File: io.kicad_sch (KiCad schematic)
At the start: 80 parts, among them IC16 MC1489, IC19 MC1488, IC23 MC1489, IC24 82C711, X7 24MHz

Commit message: prepare for fabrication
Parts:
- C108, C111, C112, C113, C114, C115, C122, C123, C125, C126, C132, C134, C136, C153, C154, C155, C156: LCSC (none) -> C1790; LCSC Part (none) -> C1790
- C127, C133, C135, C141, C142, C143, C144, C145: LCSC (none) -> C46653; LCSC Part (none) -> C46653
- C128, C129: LCSC (none) -> C1804; LCSC Part (none) -> C1804
- C137, C146: LCSC (none) -> C344201; LCSC Part (none) -> C344201
- C147, C158: LCSC (none) -> C49678; LCSC Part (none) -> C49678
- C149: LCSC (none) -> C2987938; LCSC Part (none) -> C2987938
- IC16, IC23: LCSC (none) -> C3199481; LCSC Part (none) -> C3199481
- IC19: LCSC (none) -> C3213152; LCSC Part (none) -> C3213152
- R116, R117, R118, R121, R122, R123, R126, R131, R138, R140, R141: LCSC (none) -> C2907326; LCSC Part (none) -> C2907326
- R119: LCSC (none) -> C2907219; LCSC Part (none) -> C2907219
- R120: LCSC (none) -> C17634; LCSC Part (none) -> C17634
- R127: LCSC (none) -> C5713328; LCSC Part (none) -> C5713328
- R128: LCSC (none) -> C2090916; LCSC Part (none) -> C2090916
- R129: LCSC (none) -> C2933293; LCSC Part (none) -> C2933293
- R139, R142, R143, R144, R145: LCSC (none) -> C2907232; LCSC Part (none) -> C2907232
- R215: LCSC (none) -> C17477; LCSC Part (none) -> C17477
- RP8, RP9: value 33R -> 33Rx8; LCSC (none) -> C1739831; LCSC Part (none) -> C1739831
- TP10, TP11, TP5, TP8, TP9: now not fitted

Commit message: update design to correct errors found by IanJ
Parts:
- X7: footprint Crystal:Crystal_HC50_Horizontal_1EP_style2 -> Crystal:Crystal_HC49-U_Horizontal_1EP_style2
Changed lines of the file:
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@@
 			)
 		)
-		(property "Footprint" "Crystal:Crystal_HC50_Horizontal_1EP_style2"
+		(property "Footprint" "Crystal:Crystal_HC49-U_Horizontal_1EP_style2"
 			(at 106.68 228.6 0)
 			(effects

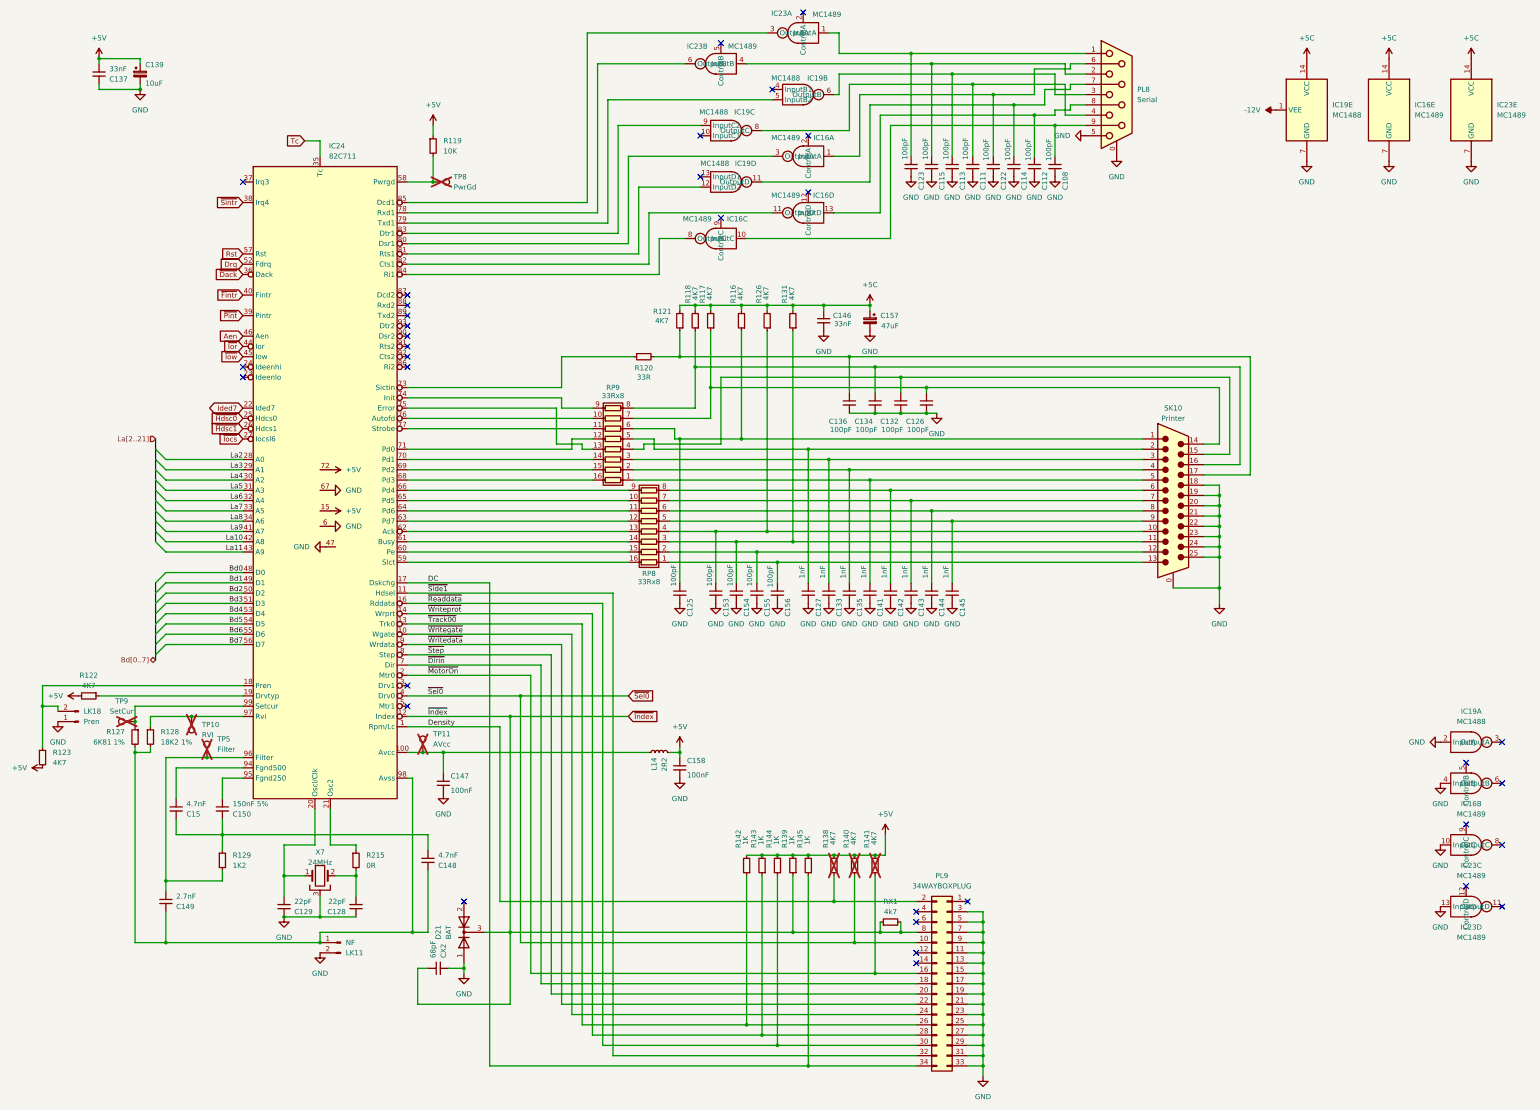
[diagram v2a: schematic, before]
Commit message: verify all component values vs TRM
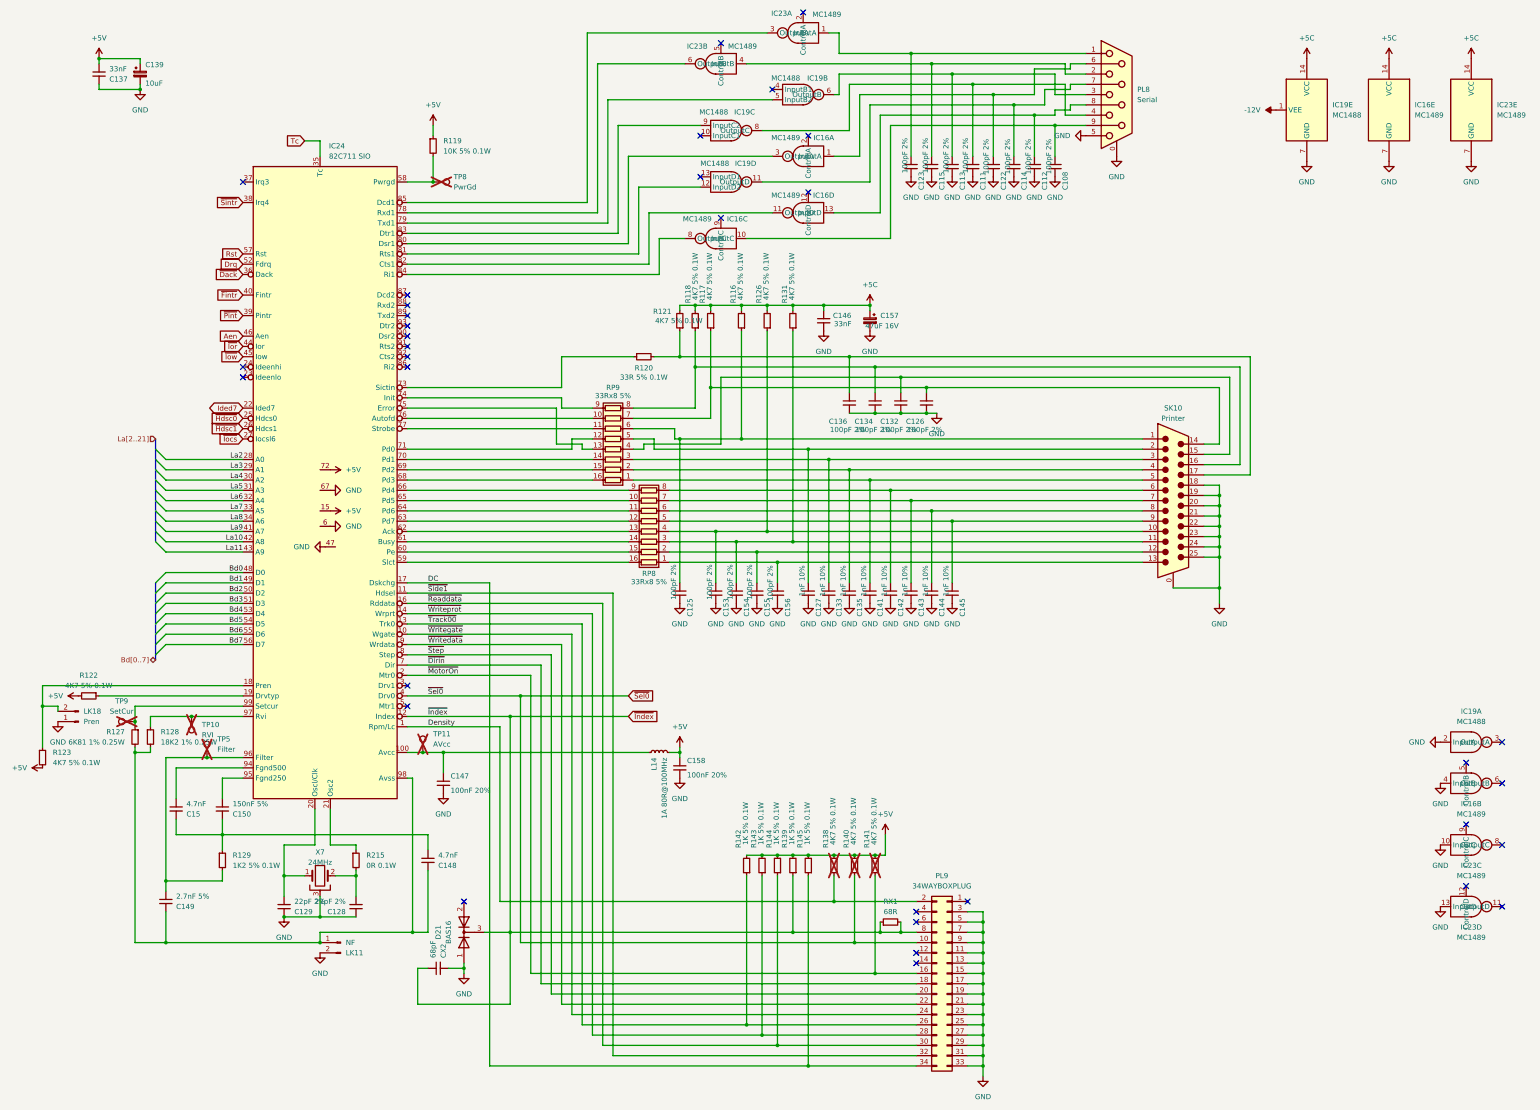
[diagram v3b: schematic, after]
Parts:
- C108, C111, C112, C113, C114, C115, C122, C123, C125, C126, C132, C134, C136, C153, C154, C155, C156: value 100pF -> 100pF 2%
- C127, C133, C135, C141, C142, C143, C144, C145: value 1nF -> 1nF 10%
- C128, C129: value 22pF -> 22pF 2%
- C147, C158: value 100nF -> 100nF 20%
- C149: value 2.7nF -> 2.7nF 5%
- C157: value 47uF -> 47uF 16V
- D21: value BAT -> BAS16
- IC24: value 82C711 -> 82C711 SIO
- L14: value 2R2 -> 1A 80R@100MHz
- R116, R117, R118, R121, R122, R123, R126, R131, R138, R140, R141: value 4K7 -> 4K7 5% 0.1W
- R119: value 10K -> 10K 5% 0.1W
- R120: value 33R -> 33R 5% 0.1W
- R127: value 6K81 1% -> 6K81 1% 0.25W
- R128: value 18K2 1% -> 18K2 1% 0.25W
- R129: value 1K2 -> 1K2 5% 0.1W
- R139, R142, R143, R144, R145: value 1K -> 1K 5% 0.1W
- R215: value 0R -> 0R 0.1W
- RP8, RP9: value 33Rx8 -> 33Rx8 5%
- RX1: value 4k7 -> 68R
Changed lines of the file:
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@@
 			)
 		)
-		(property "Value" "100pF"
+		(property "Value" "100pF 2%"
 			(at 281.686 46.482 90)
 			(effects
@@
 			)
 		)
-		(property "Value" "4K7"
+		(property "Value" "4K7 5% 0.1W"
 			(at 189.484 91.44 0)
 			(effects
@@
 			)
 		)
-		(property "Value" "1K2"
+		(property "Value" "1K2 5% 0.1W"
 			(at 85.09 226.0599 0)
 			(effects
@@
 			)
 		)
-		(property "Value" "1nF"
+		(property "Value" "1nF 10%"
 			(at 241.046 151.892 90)
 			(effects
@@
 			)
 		)
-		(property "Value" "4K7"
+		(property "Value" "4K7 5% 0.1W"
 			(at 238.506 220.98 90)
 			(effects
@@
 			)
 		)
-		(property "Value" "1K"
+		(property "Value" "1K 5% 0.1W"
 			(at 223.266 220.98 90)
 			(effects
@@
 			)
 		)
-		(property "Value" "100pF"
+		(property "Value" "100pF 2%"
 			(at 276.606 46.482 90)
 			(effects
@@
 			)
 		)
-		(property "Value" "100pF"
+		(property "Value" "100pF 2%"
 			(at 202.946 151.638 90)
 			(effects
@@
 			)
 		)
-		(property "Value" "BAT"
+		(property "Value" "BAS16"
 			(at 138.43 242.57 0)
 			(effects
@@
 			)
 		)
-		(property "Value" "100pF"
+		(property "Value" "100pF 2%"
 			(at 194.056 151.638 90)
 			(effects
@@
 			)
 		)
-		(property "Value" "4K7"
+		(property "Value" "4K7 5% 0.1W"
 			(at 49.53 181.61 90)
 			(effects
@@
 			)
 		)
-		(property "Value" "4K7"
+		(property "Value" "4K7 5% 0.1W"
 			(at 223.266 86.36 90)
 			(effects
@@
 			)
 		)
-		(property "Value" "100pF"
+		(property "Value" "100pF 2%"
 			(at 271.272 46.482 90)
 			(effects
@@
 			)
 		)
-		(property "Value" "2.7nF"
+		(property "Value" "2.7nF 5%"
 			(at 71.12 233.6865 0)
 			(effects
@@
 			)
 		)
-		(property "Value" "100pF"
+		(property "Value" "100pF 2%"
 			(at 256.286 46.228 90)
 			(effects
@@
 			)
 		)
-		(property "Value" "100pF"
+		(property "Value" "100pF 2%"
 			(at 261.366 46.228 90)
 			(effects
@@
 			)
 		)
-		(property "Value" "4K7"
+		(property "Value" "4K7 5% 0.1W"
 			(at 202.946 86.36 90)
 			(effects
@@
 			)
 		)
-		(property "Value" "4K7"
+		(property "Value" "4K7 5% 0.1W"
 			(at 216.916 86.36 90)
 			(effects
@@
 			)
 		)
-		(property "Value" "100pF"
+		(property "Value" "100pF 2%"
 			(at 266.192 46.228 90)
 			(effects
@@
 			)
 		)
-		(property "Value" "100pF"
+		(property "Value" "100pF 2%"
 			(at 251.714 118.3575 0)
 			(effects
@@
 			)
 		)
-		(property "Value" "18K2 1%"
+		(property "Value" "18K2 1% 0.25W"
 			(at 67.31 195.5799 0)
 			(effects
@@
 			)
 		)
-		(property "Value" "6K81 1%"
+		(property "Value" "6K81 1% 0.25W"
 			(at 58.42 195.5799 0)
 			(effects
@@
 			)
 		)
-		(property "Value" "33Rx8"
+		(property "Value" "33Rx8 5%"
 			(at 179.07 109.982 90)
 			(effects
@@
 			)
 		)
-		(property "Value" "33R"
+		(property "Value" "33R 5% 0.1W"
 			(at 186.69 105.41 90)
 			(effects
@@
 			)
 		)
-		(property "Value" "100pF"
+		(property "Value" "100pF 2%"
 			(at 217.932 151.892 90)
 			(effects
@@
 			)
 		)
-		(property "Value" "100pF"
+		(property "Value" "100pF 2%"
 			(at 245.364 118.3575 0)
 			(effects
@@
 			)
 		)
-		(property "Value" "1K"
+		(property "Value" "1K 5% 0.1W"
 			(at 211.836 220.98 90)
 			(effects
@@
 			)
 		)
-		(property "Value" "4K7"
+		(property "Value" "4K7 5% 0.1W"
 			(at 243.586 220.98 90)
 			(effects
@@
 			)
 		)
-		(property "Value" "100pF"
+		(property "Value" "100pF 2%"
 			(at 208.026 151.638 90)
 			(effects
@@
 			)
 		)
-		(property "Value" "1nF"
+		(property "Value" "1nF 10%"
 			(at 261.366 151.892 90)
 			(effects
@@
 			)
 		)
-		(property "Value" "1nF"
+		(property "Value" "1nF 10%"
 			(at 230.886 151.892 90)
 			(effects
@@
 			)
 		)
-		(property "Value" "4K7"
+		(property "Value" "4K7 5% 0.1W"
 			(at 233.426 220.98 90)
 			(effects
@@
 			)
 		)
-		(property "Value" "1nF"
+		(property "Value" "1nF 10%"
 			(at 251.206 151.892 90)
 			(effects
@@
 			)
 		)
-		(property "Value" "100pF"
+		(property "Value" "100pF 2%"
 			(at 232.664 118.3575 0)
 			(effects
@@
 			)
 		)
-		(property "Value" "4K7"
+		(property "Value" "4K7 5% 0.1W"
 			(at 40.64 200.6599 0)
 			(effects
@@
 			)
 		)
-		(property "Value" "4K7"
+		(property "Value" "4K7 5% 0.1W"
 			(at 210.566 86.36 90)
 			(effects
@@
 			)
 		)
-		(property "Value" "1K"
+		(property "Value" "1K 5% 0.1W"
 			(at 215.646 220.98 90)
 			(effects
@@
 			)
 		)
-		(property "Value" "1K"
+		(property "Value" "1K 5% 0.1W"
 			(at 219.456 220.98 90)
 			(effects
@@
 			)
 		)
-		(property "Value" "1nF"
+		(property "Value" "1nF 10%"
 			(at 256.286 151.892 90)
 			(effects
@@
 			)
 		)
-		(property "Value" "82C711"
+		(property "Value" "82C711 SIO"
 			(at 108.8741 50.8 0)
 			(effects
@@
 			)
 		)
-		(property "Value" "1K"
+		(property "Value" "1K 5% 0.1W"
 			(at 227.076 220.98 90)
 			(effects
@@
 			)
 		)
-		(property "Value" "1nF"
+		(property "Value" "1nF 10%"
 			(at 235.966 151.892 90)
 			(effects
@@
 			)
 		)
-		(property "Value" "33Rx8"
+		(property "Value" "33Rx8 5%"
 			(at 187.96 155.956 90)
 			(effects
@@
 			)
 		)
-		(property "Value" "100pF"
+		(property "Value" "100pF 2%"
 			(at 251.206 46.228 90)
 			(effects
@@
 			)
 		)
-		(property "Value" "100pF"
+		(property "Value" "100pF 2%"
 			(at 212.852 151.638 90)
 			(effects
@@
 			)
 		)
-		(property "Value" "100nF"
+		(property "Value" "100nF 20%"
 			(at 138.938 207.518 0)
 			(effects
@@
 			)
 		)
-		(property "Value" "0R"
+		(property "Value" "0R 0.1W"
 			(at 118.11 226.0599 0)
 			(effects
@@
 			)
 		)
-		(property "Value" "100pF"
+		(property "Value" "100pF 2%"
 			(at 286.766 46.482 90)
 			(effects
@@
 			)
 		)
-		(property "Value" "2R2"
+		(property "Value" "1A 80R@100MHz"
 			(at 191.7699 199.39 0)
 			(effects
@@
 			)
 		)
-		(property "Value" "10K"
+		(property "Value" "10K 5% 0.1W"
 			(at 137.16 49.5299 0)
 			(effects
@@
 			)
 		)
-		(property "Value" "1nF"
+		(property "Value" "1nF 10%"
 			(at 225.806 151.892 90)
 			(effects
@@
 			)
 		)
-		(property "Value" "22pF"
+		(property "Value" "22pF 2%"
 			(at 113.03 234.9565 0)
 			(effects
@@
 			)
 		)
-		(property "Value" "4k7"
+		(property "Value" "68R"
 			(at 247.65 237.49 90)
 			(effects
@@
 			)
 		)
-		(property "Value" "47uF"
+		(property "Value" "47uF 16V"
 			(at 249.682 92.71 0)
 			(effects
@@
 			)
 		)
-		(property "Value" "100nF"
+		(property "Value" "100nF 20%"
 			(at 197.358 203.708 0)
 			(effects
@@
 			)
 		)
-		(property "Value" "4K7"
+		(property "Value" "4K7 5% 0.1W"
 			(at 199.39 86.36 90)
 			(effects
@@
 			)
 		)
-		(property "Value" "1nF"
+		(property "Value" "1nF 10%"
 			(at 246.126 151.892 90)
 			(effects
@@
 			)
 		)
-		(property "Value" "100pF"
+		(property "Value" "100pF 2%"
 			(at 239.014 118.3575 0)
 			(effects
@@
 			)
 		)
-		(property "Value" "22pF"
+		(property "Value" "22pF 2%"
 			(at 100.33 234.9565 0)
 			(effects

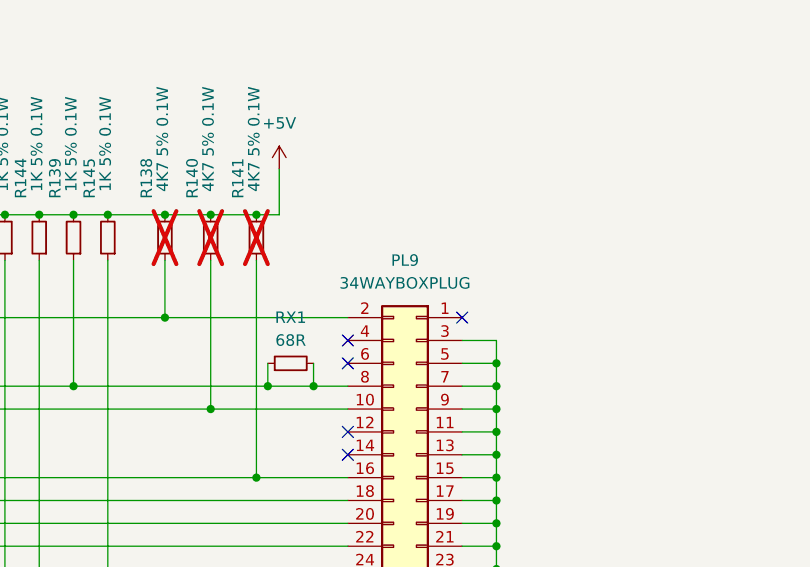
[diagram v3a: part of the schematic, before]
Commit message: refine edge port mounting positions
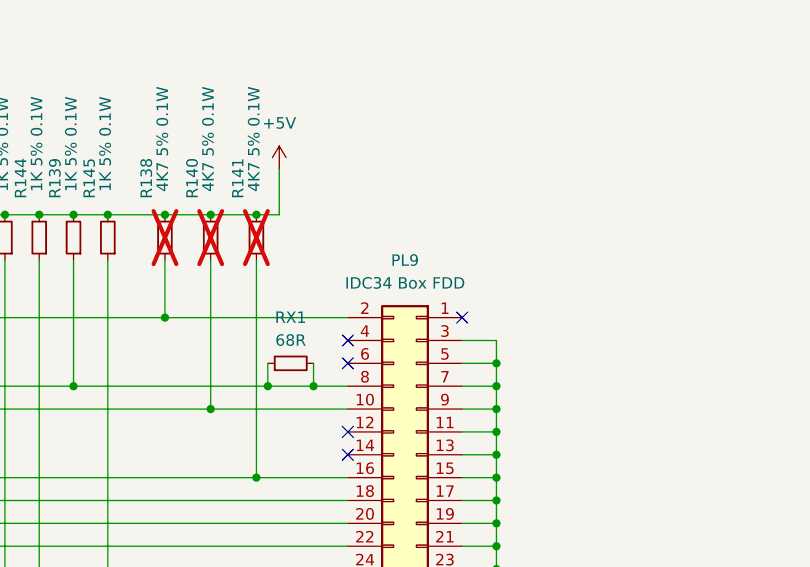
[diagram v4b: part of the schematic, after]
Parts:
- PL9: value 34WAYBOXPLUG -> IDC34 Box FDD
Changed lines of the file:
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@@
 			)
 		)
-		(property "Value" "34WAYBOXPLUG"
+		(property "Value" "IDC34 Box FDD"
 			(at 260.35 231.14 0)
 			(effects

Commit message: fix qfp footprints, restore CAS filters
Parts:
- IC24: footprint Package_QFP:PQFP-100_14x20mm_P0.65mm -> Acorn:PQFP-100_14x20mm_P0.65mm
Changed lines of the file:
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@@
 			)
 		)
-		(property "Footprint" "Package_QFP:PQFP-100_14x20mm_P0.65mm"
+		(property "Footprint" "Acorn:PQFP-100_14x20mm_P0.65mm"
 			(at 106.68 120.65 0)
 			(effects
